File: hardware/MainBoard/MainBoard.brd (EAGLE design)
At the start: 90 x 56 mm, 265 parts, among them J1 CON-71741-2184-BOT, J2 CON-71741-2184-TOP, J3 CON-FTSH-105-01-L-DV-K, J4 CON-ZX62R-B-5P, J7 CON-RJ45-J0G-0007NL, J8 SWITCH-CJS-1200-1200, M1 MOUNT-HOLE3.3, M2 MOUNT-HOLE3.3, M3 MOUNT-HOLE3.3, M4 MOUNT-HOLE3.3, M5 FIDUCIAL1X2, M6 FIDUCIAL1X2, M7 FIDUCIAL1X2, M8 FIDUCIAL1X2, Q1 MMBT3904, SW1 SWITCH-ESWITCH-TL3340G, SW2 SWITCH-ESWITCH-TL3340G, U1 A2F500M3G-1FGG256, U2 MAX19706-T4877-4, U3 MAX19706-T4877-4, U4 USBLC6-2SC6, U5 FT232HL, U6 DP83848C-VBH48A, U7 93LC56BT-OT, U8 DS1818-10-SOT-23, X1 ECX-2236-200, X2 ECX-31B, X3 ASEM1-C, X5 ECX-42-120

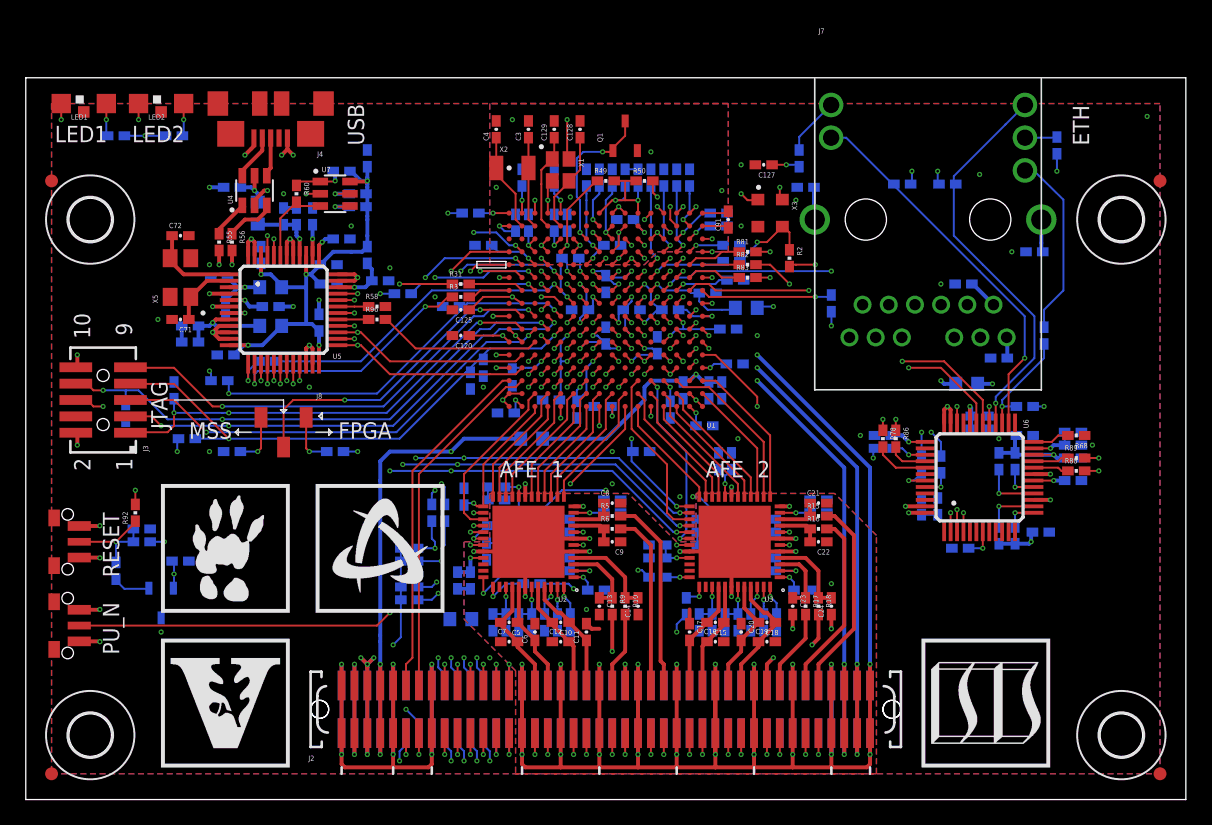
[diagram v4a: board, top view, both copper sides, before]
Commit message: Added AGND and DGND test points.
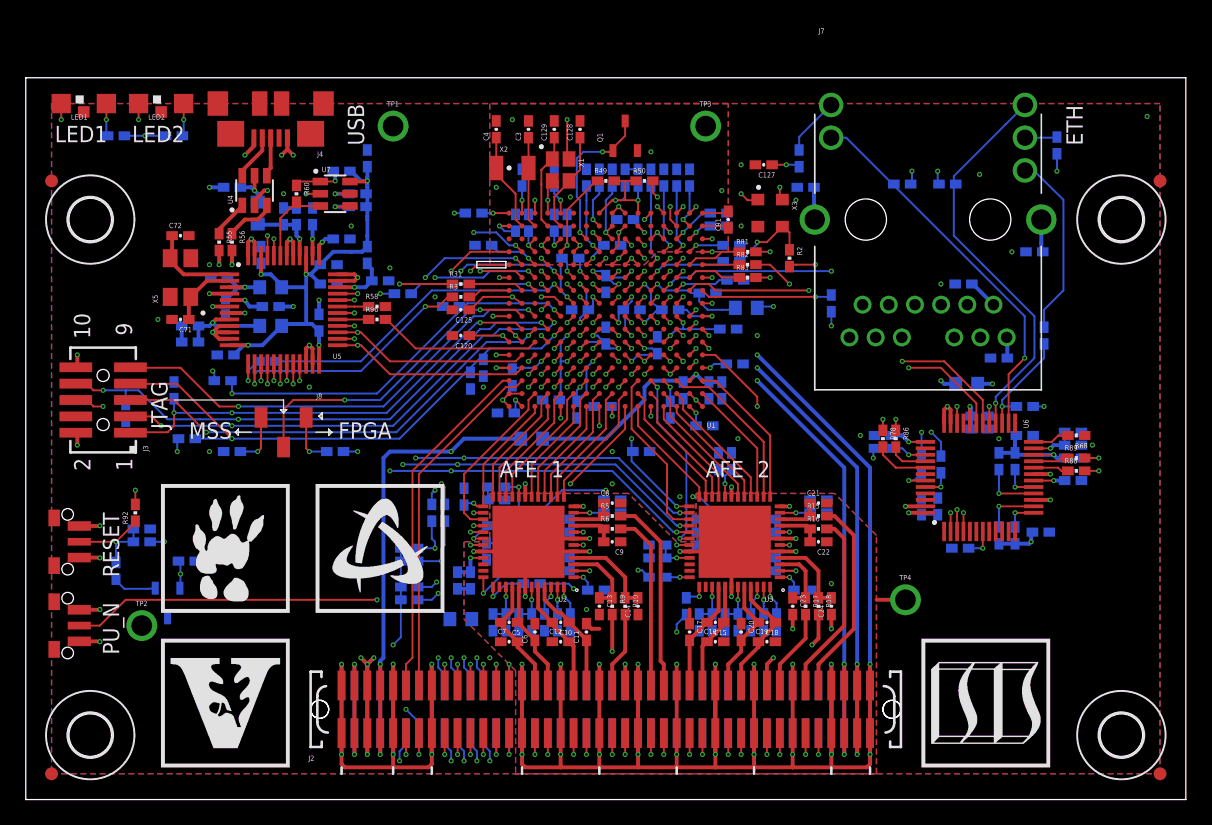
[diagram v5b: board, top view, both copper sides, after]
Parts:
- added TP1, TP2: TESTPOINT-YELLOW, MainBoard:TESTPOINT
- added TP3, TP4: TESTPOINT-GREEN, MainBoard:TESTPOINT
- moved C130 0.50 mm to (12.5, 18.5)
- moved U8 0.50 mm to (11.0, 15.2)
- moved R8 0.25 mm to (15.3, 32.5)
- moved R94 0.25 mm to (34.8, 45.5)
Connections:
- net AGND: now also TP3.1, TP4.1
- net DGND: now also TP1.1, TP2.1
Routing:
- net AGND: track 264.3 -> 266.5 mm
- net !WAKEUP: track 80.7 -> 79.9 mm
- net DGND: vias 99 -> 98

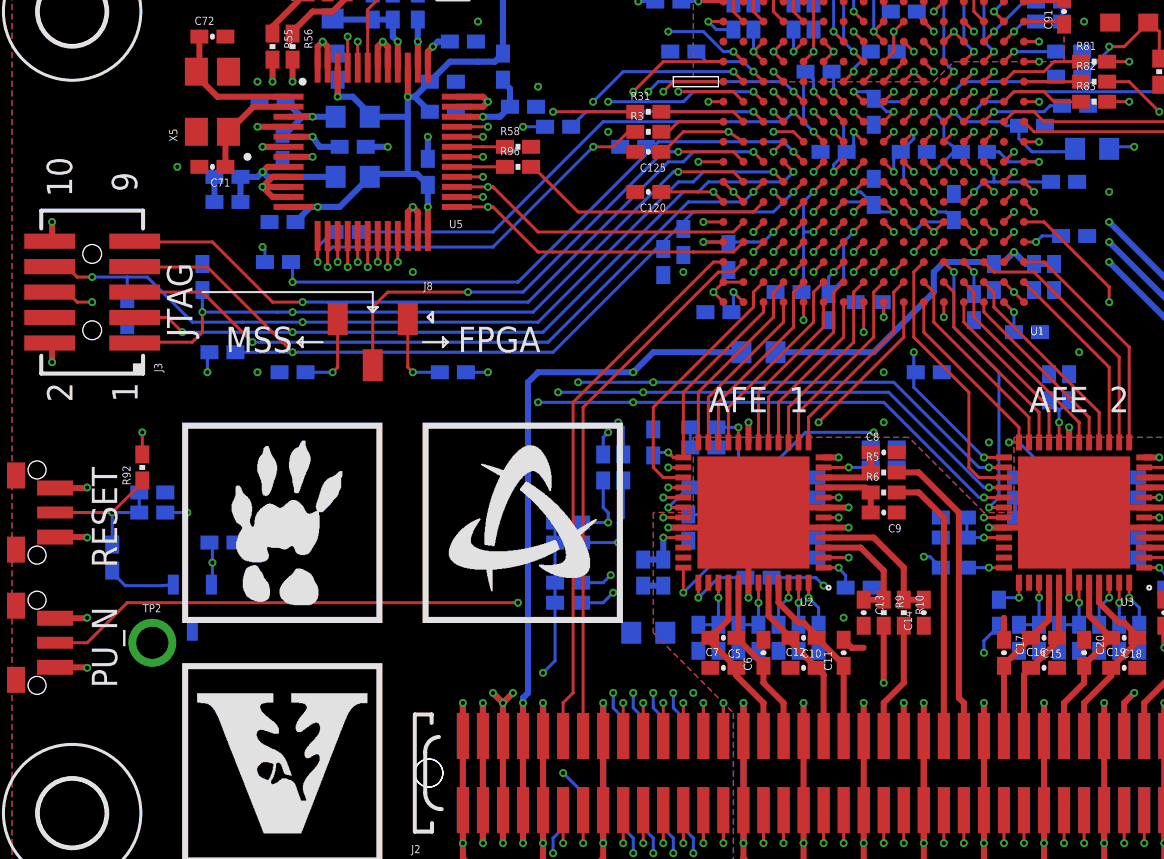
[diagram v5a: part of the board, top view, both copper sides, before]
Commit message: Finished the silkscreen layers.
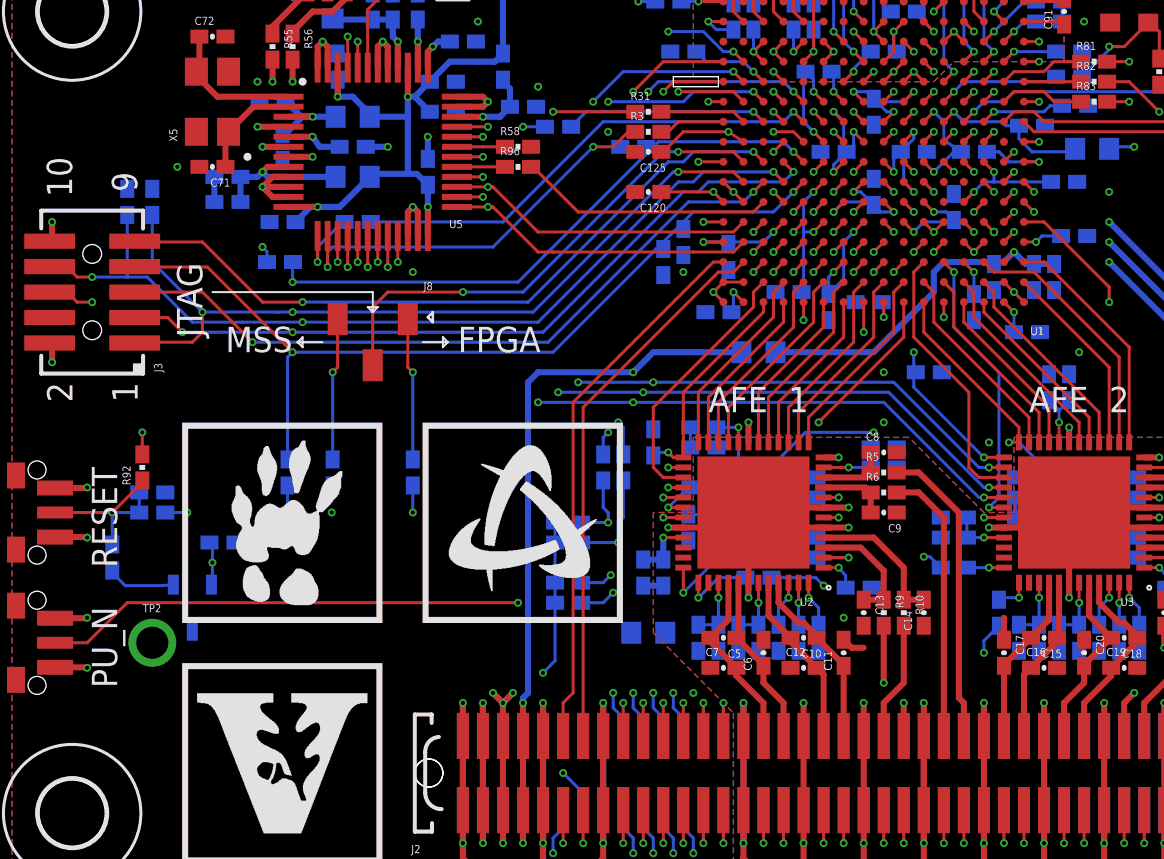
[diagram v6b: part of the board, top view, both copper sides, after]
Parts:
- moved R7 6.82 mm to (15.8, 22.0), turned to 270 degrees
- moved R64 5.50 mm to (7.75, 35.5), turned to 270 degrees
- moved R66 5.39 mm to (18.0, 22.0), turned to 90 degrees
- moved R67 5.39 mm to (22.0, 22.0), turned to 270 degrees
- moved R65 4.51 mm to (9.00, 35.5)
- moved R4 0.71 mm to (19.2, 34.5)
- moved R8 0.10 mm to (15.4, 32.5)
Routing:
- net TCK: track 35.8 -> 40.6 mm
- net MSSTAP: track 4.10 -> 7.10 mm
- net FPGATAP: track 4.10 -> 7.10 mm
- net VPUMP: track 42.4 -> 45.0 mm
- net TRST: track 42.2 -> 44.2 mm
- net UART0_RXD: track 24.8 -> 24.1 mm
- net USB_DB0: track 37.8 -> 38.5 mm
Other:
- board text added: ">REVISION"
- board text added: ">TITLE"
- board text added: "Copyright c 2012"
- board text added: "Mixed-signal module"
- board text added: "Rev"
- board text added: "Vanderbilt University, ISIS"
- board text added: "for the Marmote platform"
- board text added: "http://marmote.googlecode.com"

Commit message: Backup before re-numbering components on schematic.
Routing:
- net AFE1_T/!R: track 13.2 -> 13.0 mm, vias 0 -> 1
- net AFE2_T/!R: track 13.6 -> 13.4 mm, vias 0 -> 1
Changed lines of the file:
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@@
 <setting verticaltext="up"/>
 </settings>
-<grid distance="1" unitdist="mm" unit="mm" style="lines" multiple="1" display="yes" altdistance="0.1" altunitdist="mm" altunit="mm"/>
+<grid distance="1" unitdist="mm" unit="mm" style="lines" multiple="1" display="yes" altdistance="0.25" altunitdist="mm" altunit="mm"/>
 <layers>
-<layer number="1" name="Top" color="4" fill="1" visible="no" active="yes"/>
+<layer number="1" name="Top" color="4" fill="1" visible="yes" active="yes"/>
 <layer number="2" name="GND" color="1" fill="3" visible="no" active="yes"/>
 <layer number="3" name="Inner1" color="13" fill="3" visible="no" active="yes"/>
-<layer number="14" name="Inner2" color="10" fill="6" visible="no" active="yes"/>
+<layer number="14" name="Inner2" color="10" fill="6" visible="yes" active="yes"/>
 <layer number="15" name="D3V3" color="4" fill="3" visible="no" active="yes"/>
 <layer number="16" name="Bottom" color="1" fill="1" visible="yes" active="yes"/>
@@
 <layer number="19" name="Unrouted" color="6" fill="1" visible="no" active="yes"/>
 <layer number="20" name="Dimension" color="15" fill="1" visible="yes" active="yes"/>
-<layer number="21" name="tPlace" color="7" fill="1" visible="no" active="yes"/>
-<layer number="22" name="bPlace" color="7" fill="1" visible="yes" active="yes"/>
+<layer number="21" name="tPlace" color="7" fill="1" visible="yes" active="yes"/>
+<layer number="22" name="bPlace" color="7" fill="1" visible="no" active="yes"/>
 <layer number="23" name="tOrigins" color="15" fill="1" visible="no" active="yes"/>
-<layer number="24" name="bOrigins" color="15" fill="1" visible="yes" active="yes"/>
+<layer number="24" name="bOrigins" color="15" fill="1" visible="no" active="yes"/>
 <layer number="25" name="tNames" color="7" fill="1" visible="no" active="yes"/>
 <layer number="26" name="bNames" color="7" fill="1" visible="no" active="yes"/>
 <layer number="27" name="tValues" color="7" fill="1" visible="no" active="yes"/>
 <layer number="28" name="bValues" color="7" fill="1" visible="no" active="yes"/>
-<layer number="29" name="tStop" color="7" fill="3" visible="no" active="yes"/>
-<layer number="30" name="bStop" color="7" fill="6" visible="yes" active="yes"/>
+<layer number="29" name="tStop" color="7" fill="3" visible="yes" active="yes"/>
+<layer number="30" name="bStop" color="7" fill="6" visible="no" active="yes"/>
 <layer number="31" name="tCream" color="7" fill="4" visible="no" active="yes"/>
-<layer number="32" name="bCream" color="7" fill="5" visible="yes" active="yes"/>
+<layer number="32" name="bCream" color="7" fill="5" visible="no" active="yes"/>
 <layer number="33" name="tFinish" color="6" fill="3" visible="no" active="yes"/>
 <layer number="34" name="bFinish" color="6" fill="6" visible="no" active="yes"/>
@@
 <layer number="46" name="Milling" color="3" fill="1" visible="no" active="yes"/>
 <layer number="47" name="Measures" color="7" fill="1" visible="no" active="yes"/>
-<layer number="48" name="Document" color="7" fill="1" visible="no" active="yes"/>
+<layer number="48" name="Document" color="7" fill="1" visible="yes" active="yes"/>
 <layer number="49" name="Reference" color="7" fill="1" visible="no" active="yes"/>
 <layer number="50" name="dxf" color="7" fill="1" visible="no" active="yes"/>
-<layer number="51" name="tDocu" color="14" fill="1" visible="no" active="yes"/>
+<layer number="51" name="tDocu" color="14" fill="1" visible="yes" active="yes"/>
 <layer number="52" name="bDocu" color="11" fill="1" visible="no" active="yes"/>
 <layer number="53" name="tGND_GNDA" color="7" fill="9" visible="no" active="no"/>
@@
 <contactref element="U2" pad="27"/>
 <wire x1="35.5" y1="21.75" x2="34.5" y2="21.75" width="0.1524" layer="1"/>
-<wire x1="34.5" y1="21.75" x2="34" y2="22.25" width="0.1524" layer="1"/>
-<wire x1="34" y1="22.25" x2="34" y2="25.25" width="0.1524" layer="1"/>
-<wire x1="34" y1="25.25" x2="39" y2="30.25" width="0.1524" layer="1"/>
+<wire x1="34.5" y1="21.75" x2="34.25" y2="22" width="0.1524" layer="1"/>
+<wire x1="34.25" y1="22" x2="34.25" y2="25.5" width="0.1524" layer="1"/>
+<wire x1="34.25" y1="25.5" x2="39" y2="30.25" width="0.1524" layer="1"/>
 <contactref element="U1" pad="B14"/>
 <wire x1="39" y1="30.25" x2="39" y2="31" width="0.1524" layer="1"/>
 <wire x1="39" y1="31" x2="39.5" y2="31.5" width="0.1524" layer="1"/>
+<via x="34.5" y="21.75" extent="1-16" drill="0.2032" alwaysstop="yes"/>
 </signal>
 <signal name="!AFE2_SHDN">
@@
 <signal name="AFE2_T/!R">
 <contactref element="U3" pad="27"/>
-<wire x1="51.5" y1="21.75" x2="50.25" y2="21.75" width="0.1524" layer="1"/>
+<wire x1="51.5" y1="21.75" x2="50.5" y2="21.75" width="0.1524" layer="1"/>
 <contactref element="U1" pad="C6"/>
 <wire x1="47.5" y1="32.5" x2="47" y2="32" width="0.1524" layer="1"/>
 <wire x1="47" y1="32" x2="47" y2="28.75" width="0.1524" layer="1"/>
-<wire x1="47" y1="28.75" x2="49.75" y2="26" width="0.1524" layer="1"/>
-<wire x1="49.75" y1="26" x2="49.75" y2="22.25" width="0.1524" layer="1"/>
-<wire x1="49.75" y1="22.25" x2="50.25" y2="21.75" width="0.1524" layer="1"/>
+<wire x1="47" y1="28.75" x2="50" y2="25.75" width="0.1524" layer="1"/>
+<wire x1="50" y1="25.75" x2="50" y2="22.25" width="0.1524" layer="1"/>
+<wire x1="50" y1="22.25" x2="50.5" y2="21.75" width="0.1524" layer="1"/>
+<via x="50.5" y="21.75" extent="1-16" drill="0.2032" alwaysstop="yes"/>
 </signal>
 <signal name="SPI1_SS">
@@
 <via x="50.5" y="20.75" extent="1-16" drill="0.2032"/>
 <wire x1="28.25" y1="25.5" x2="28.25" y2="16" width="0.1524" layer="14"/>
-<wire x1="50.5" y1="20.75" x2="50.25" y2="20.75" width="0.1524" layer="16"/>
-<wire x1="50.25" y1="20.75" x2="45.5" y2="25.5" width="0.1524" layer="16"/>
-<wire x1="45.5" y1="25.5" x2="33" y2="25.5" width="0.1524" layer="16"/>
+<wire x1="50.5" y1="20.75" x2="50" y2="20.75" width="0.1524" layer="16"/>
+<wire x1="50" y1="20.75" x2="45.25" y2="25.5" width="0.1524" layer="16"/>
+<wire x1="45.25" y1="25.5" x2="33" y2="25.5" width="0.1524" layer="16"/>
 <via x="34.5" y="20.75" extent="1-16" drill="0.2032"/>
 <contactref element="J2" pad="18"/>
@@
 <wire x1="35.5" y1="40.5" x2="31.75" y2="40.5" width="0.1524" layer="16"/>
 <via x="31.75" y="40.5" extent="1-16" drill="0.2032"/>
-<wire x1="34.5" y1="20.75" x2="33" y2="22.25" width="0.1524" layer="14"/>
-<wire x1="33" y1="22.25" x2="33" y2="25.5" width="0.1524" layer="14"/>
+<wire x1="34.5" y1="20.75" x2="34" y2="20.75" width="0.1524" layer="14"/>
+<wire x1="34" y1="20.75" x2="33" y2="21.75" width="0.1524" layer="14"/>
+<wire x1="33" y1="21.75" x2="33" y2="25.5" width="0.1524" layer="14"/>
 <via x="33" y="25.5" extent="1-16" drill="0.2032" alwaysstop="yes"/>
 </signal>
@@
 <wire x1="33.5" y1="12.25" x2="29.25" y2="16.5" width="0.1524" layer="14"/>
 <via x="50.75" y="21.25" extent="1-16" drill="0.2032"/>
-<wire x1="50.75" y1="21.25" x2="50.5" y2="21.25" width="0.1524" layer="16"/>
-<wire x1="50.5" y1="21.25" x2="45.75" y2="26" width="0.1524" layer="16"/>
-<wire x1="45.75" y1="26" x2="33.5" y2="26" width="0.1524" layer="16"/>
+<wire x1="50.75" y1="21.25" x2="50.25" y2="21.25" width="0.1524" layer="16"/>
+<wire x1="50.25" y1="21.25" x2="45.5" y2="26" width="0.1524" layer="16"/>
+<wire x1="45.5" y1="26" x2="33.5" y2="26" width="0.1524" layer="16"/>
 <via x="34.75" y="21.25" extent="1-16" drill="0.2032"/>
 <wire x1="33.5" y1="26" x2="29.25" y2="26" width="0.1524" layer="16"/>
@@
 <wire x1="34.25" y1="41.5" x2="33.75" y2="41" width="0.1524" layer="16"/>
 <via x="33.75" y="41" extent="1-16" drill="0.2032"/>
-<wire x1="34.75" y1="21.25" x2="33.5" y2="22.5" width="0.1524" layer="14"/>
-<wire x1="33.5" y1="22.5" x2="33.5" y2="26" width="0.1524" layer="14"/>
+<wire x1="34.75" y1="21.25" x2="34.25" y2="21.25" width="0.1524" layer="14"/>
+<wire x1="34.25" y1="21.25" x2="33.5" y2="22" width="0.1524" layer="14"/>
+<wire x1="33.5" y1="22" x2="33.5" y2="26" width="0.1524" layer="14"/>
 <via x="33.5" y="26" extent="1-16" drill="0.2032" alwaysstop="yes"/>
 </signal>
